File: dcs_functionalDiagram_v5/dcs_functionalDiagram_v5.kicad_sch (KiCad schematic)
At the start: 33 parts, among them M1 Motor_DC, Q1 NMOS, U1 ${SIM.PARAMS}, U10 XOR, U2 ${SIM.PARAMS}, U3 ${SIM.PARAMS}, U4 ${SIM.PARAMS}, U5 ${SIM.PARAMS}, U6 ${SIM.PARAMS}, U7 ${SIM.PARAMS}, U8 Comp., U9 REF01CP

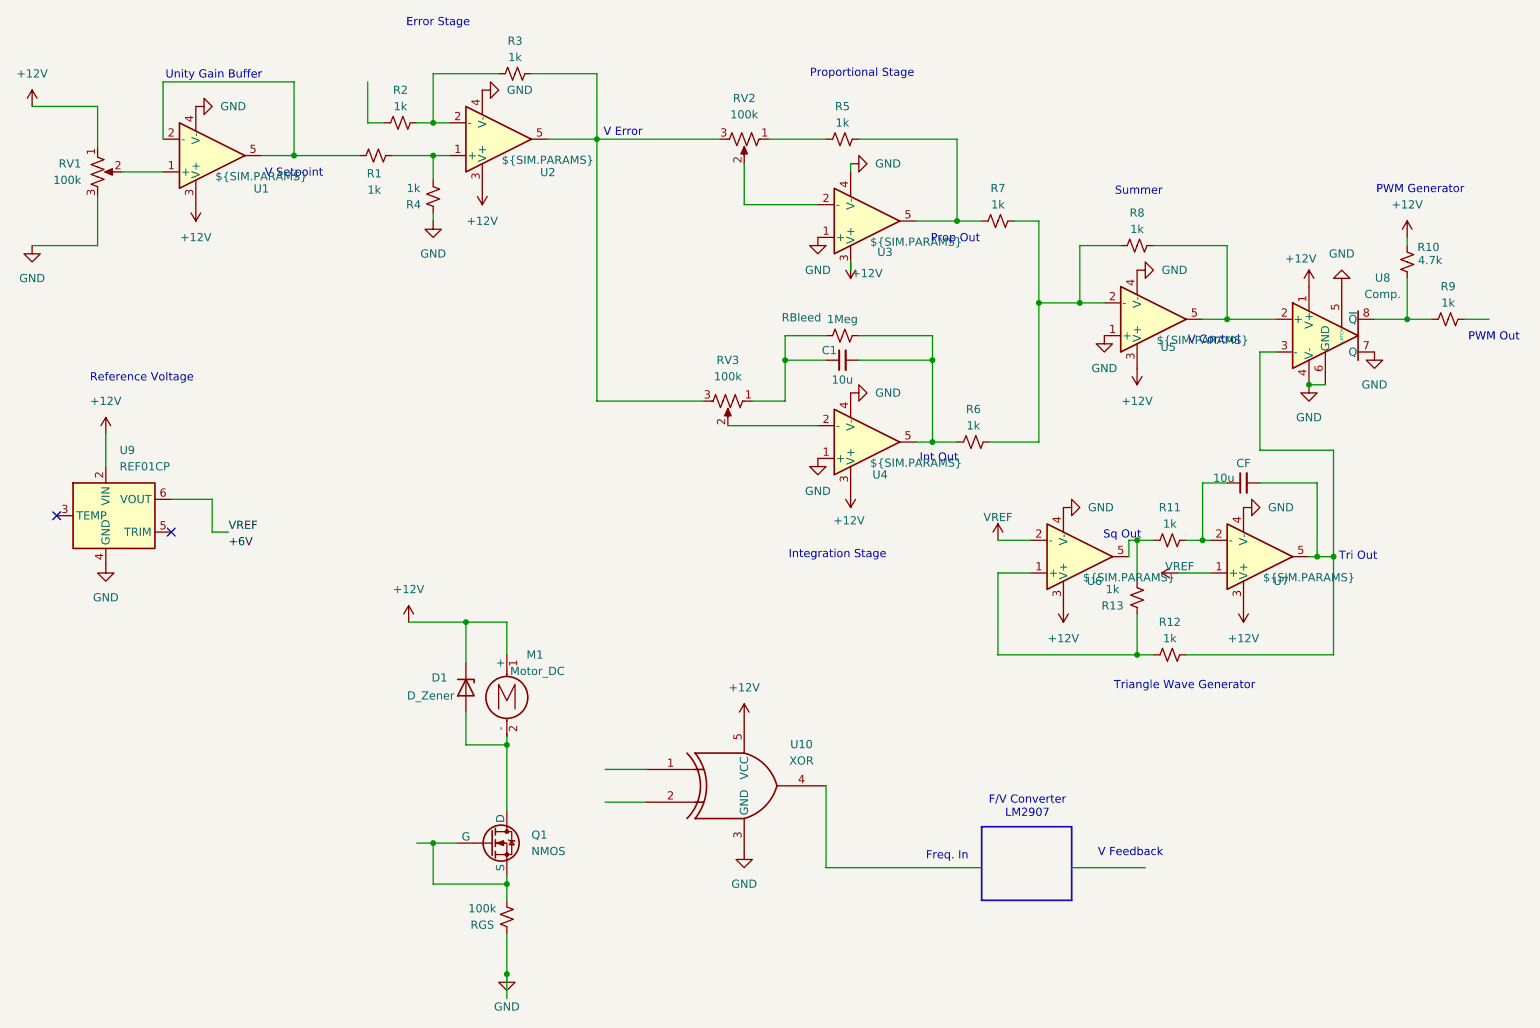
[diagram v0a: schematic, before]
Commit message: working simulink model, added resources for DC motor modeling
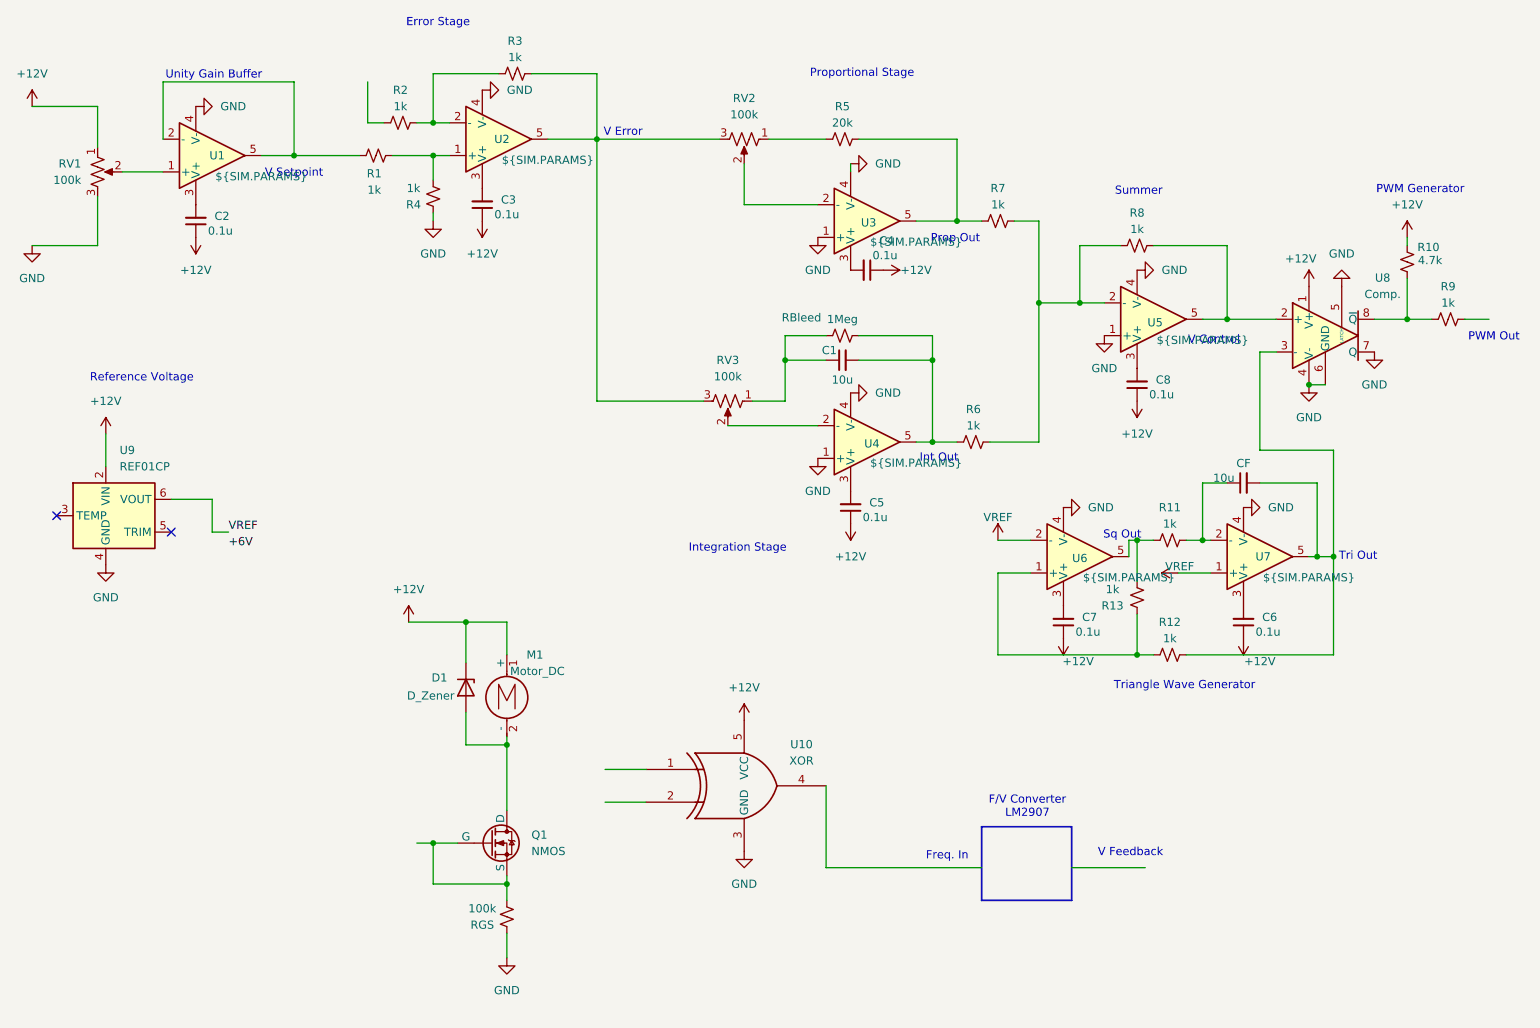
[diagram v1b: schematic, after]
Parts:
- added C2, C3, C4, C5, C6, C7, C8: 0.1u, symbol Device:C_Small
- R5: value 1k -> 20k
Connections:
- net +12V: now also C2.1, C3.1, C4.1, C5.1, C6.1, C7.1, C8.1; no longer U1.3 (V+), U2.3 (V+), U3.3 (V+), U4.3 (V+), U5.3 (V+), U6.3 (V+), U7.3 (V+)
- new net: C5.2, U4.3 (V+)
- new net: C7.2, U6.3 (V+)
- new net: C2.2, U1.3 (V+)
- new net: C4.2, U3.3 (V+)
- new net: C8.2, U5.3 (V+)
- new net: C3.2, U2.3 (V+)
- new net: C6.2, U7.3 (V+)

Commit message: pcb v1, bunch of other stuff
finished and ordered pcb v1. added datasheets to new parts we need. other stuff I forget
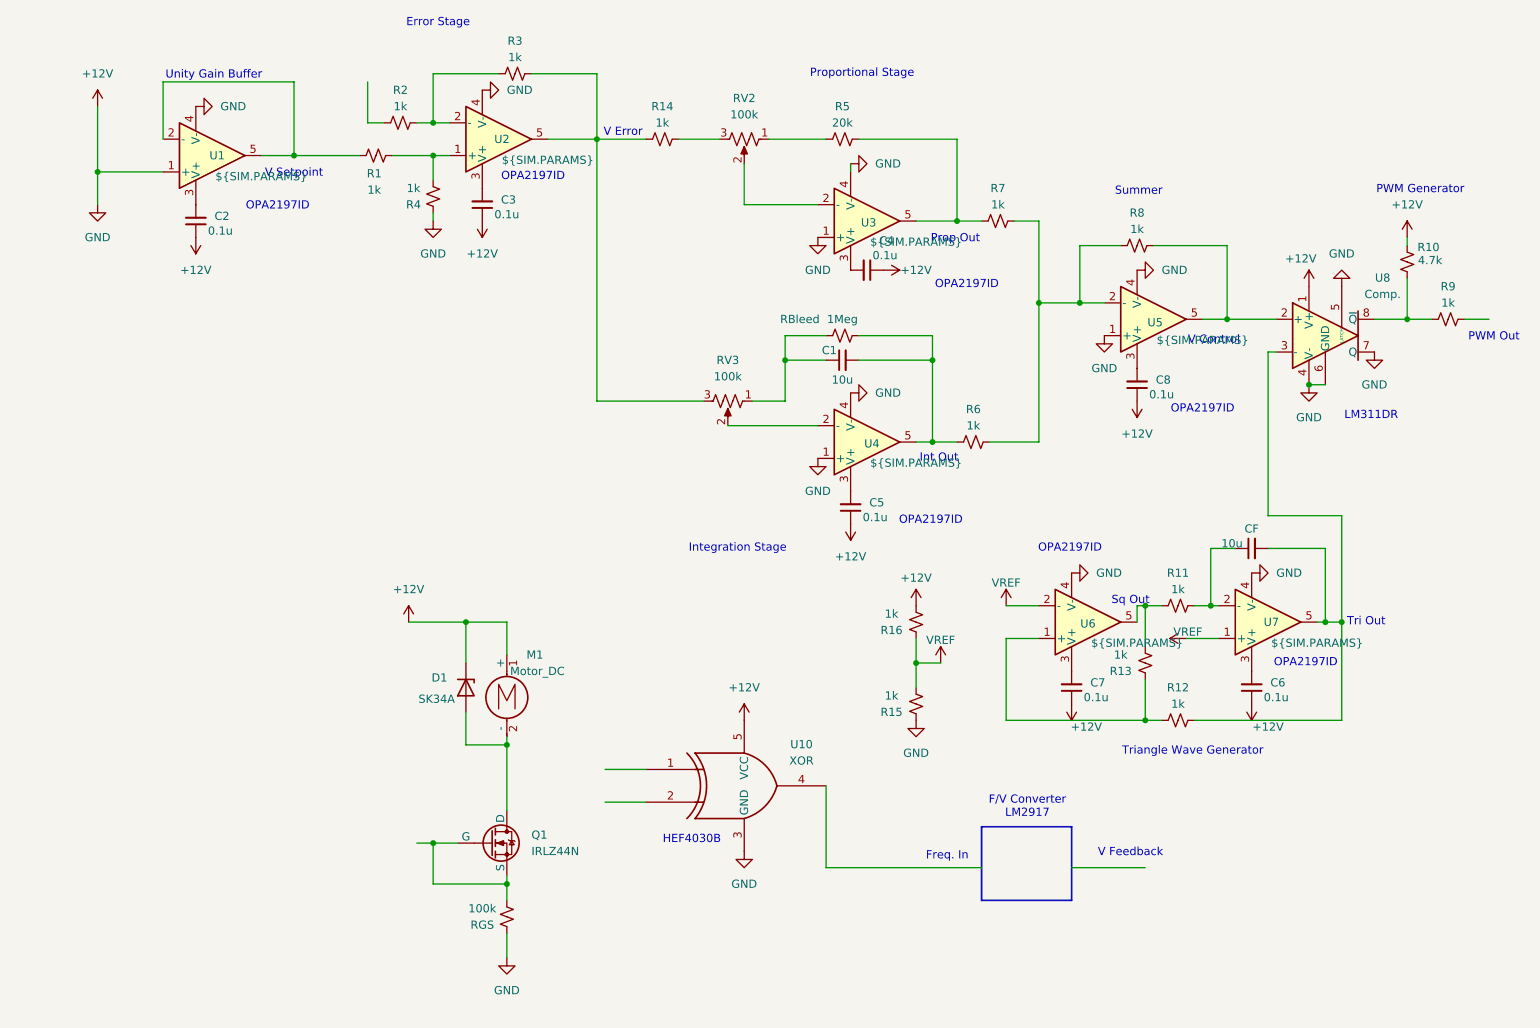
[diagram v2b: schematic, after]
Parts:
- removed RV1: 100k, symbol Device:R_Potentiometer_US
- removed U9: REF01CP, Package_DIP:DIP-8_W7.62mm, symbol Reference_Voltage:REF01CP
- added R14, R15, R16: 1k, symbol Device:R_Small_US
- D1: value D_Zener -> SK34A
- Q1: value NMOS -> IRLZ44N
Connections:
- net GND is gone; now on net +12V: R4.1, RGS.1, U1.4 (V-), U10.3 (GND), U2.4 (V-), U3.1 (+), U3.4 (V-), U4.1 (+), U4.4 (V-), U5.1 (+), U5.4 (V-), U6.4 (V-), U7.4 (V-), U8.4 (V-), U8.5 (LATCH), U8.6 (GND), U8.7 (Q)
- net +12V: now also U1.1 (+), R15.1, R16.2
- net VREF: now also R15.2, R16.1
- net at R3.2, RV3.3, U2.5: now also R14.1; no longer RV2.3
- new net: R14.2, RV2.3
- no-connect marks 2 -> 0
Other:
- note added: "F/V Converter LM2917"
- note added: "HEF4030B"
- note added: "LM311DR"
- note added: "OPA2197ID"
- note removed: "F/V Converter LM2907"
- note removed: "Reference Voltage"
- moved on the sheet: C6, C7, CF, R11, R12, R13, U6, U7
